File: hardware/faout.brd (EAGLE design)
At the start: 100 x 70 mm, 163 parts, among them IC2 MT48LC8M16A2, Q2 12MHz, Q3 MUN2214T1, Q4 MUN2214T1, Q5 ASFL, SW1 SMD_TACT_SWITCH, SW2 SMD_TACT_SWITCH, SW3 SMD_TACT_SWITCH, U1 93LC46BT-I/OT, U10 DAC8811DGK, U11 REF102AU, U12 DAC8811DGK, U13 ADR435ARZ, U14 AD8627AKSZ-R2, U15 OPA2277UA/2K5E4, U16 OPA2277UA/2K5E4, U17 MCP1700T-2502E/TT, U18 AD7980ARMZ, U2 LM3480IM3-3.3, U3 L7812ACV, U4 LM3671MF-3.3, U5 LM3671MF-1.2, U6 FLASH-SPI-25XXSMD1, U7 6SLX9TQG144, U8 AD8220ARMZ, U9 REF102AU, U99 L7912ACV

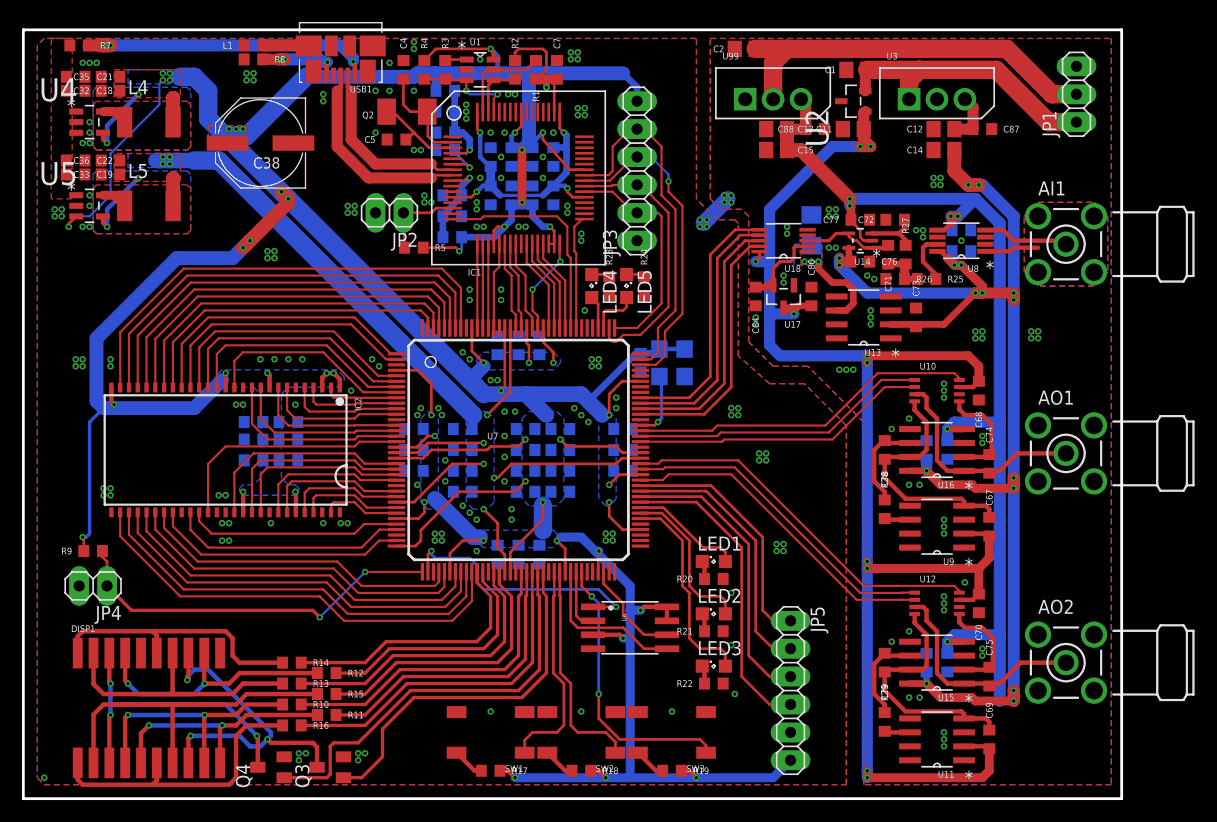
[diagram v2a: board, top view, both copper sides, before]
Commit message: Rearrange labels
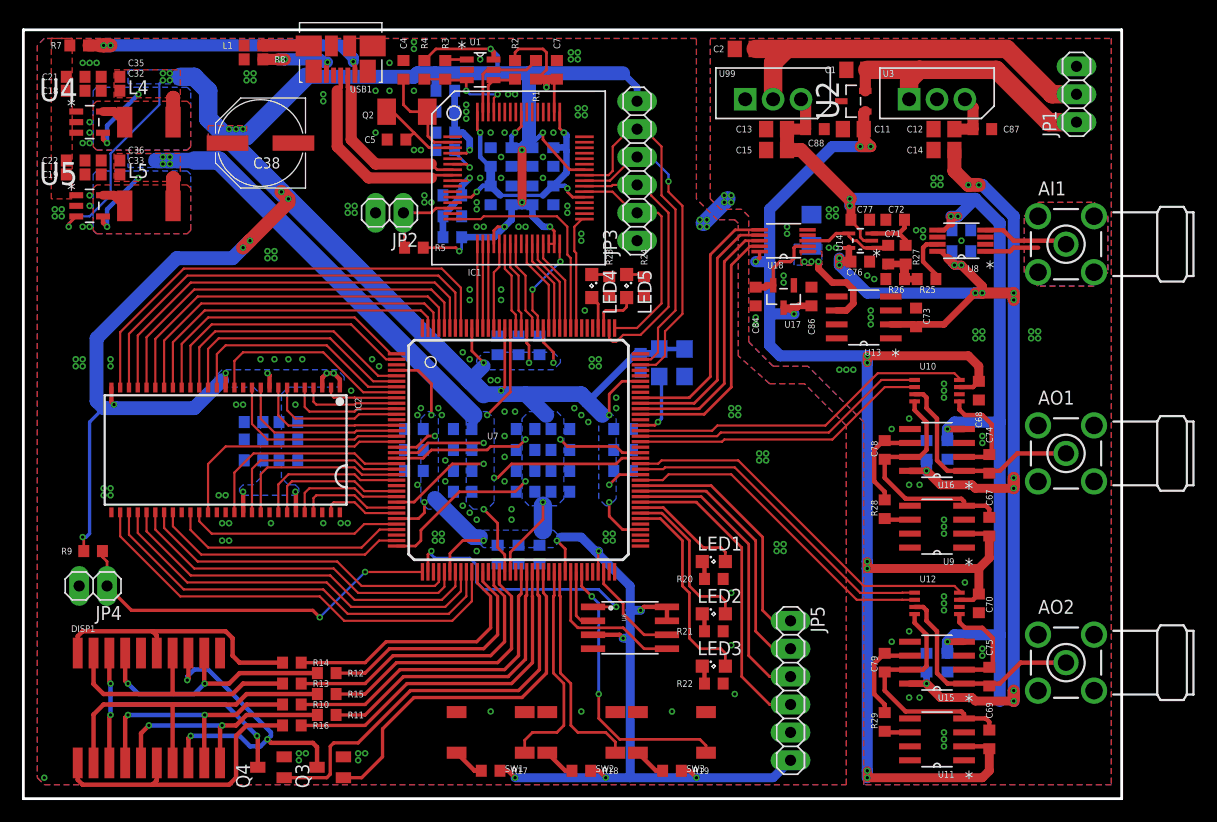
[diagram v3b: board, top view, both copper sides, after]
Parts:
- C85: device resistor:C1206 -> faout:R1206

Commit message: Cleanup and last adjustments.
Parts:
- removed C87, C88: 100nF, faout:R0603
- removed Q5: ASFL, crystal:ASF
- removed U99: L7912ACV, faout:TO254P450X1020X1935-3P
- added C8: 4.7uF, faout:R0603
- added C9: 100nF, faout:R0603
- added PWRLED1: (no value), led:SML0805
- added Q1: 12MHz, faout:TXC_QUARTZ_7A
- added R30: 2k, faout:R0603
- added U19: AD7980ARMZ, faout:SOP50P490X110-10N
- C6: value 4.7uF -> 100nF
- Q2: value 12MHz -> MUN2214T1; device faout:TXC_QUARTZ_7A -> transistor-npn:SC59-BEC
- Q4: value MUN2214T1 -> ASFL; device transistor-npn:SC59-BEC -> crystal:ASF
- R10: value 100 -> 4.7k
- R17: value 10k -> 100
- R20: value 300 -> 10k
- R25: value 7.47k -> 300
- R27: value 134k -> 7.47k
- R28: value 2k -> 134k
- R7: value 0 -> 300
- R9: value 4.7k -> 0
- U10, U12: value DAC8811DGK -> REF102AU; device faout:MSOP-8 -> faout:SOIC127P600X175-8N
- U11: value REF102AU -> DAC8811DGK; device faout:SOIC127P600X175-8N -> faout:MSOP-8
- U13: value ADR435ARZ -> DAC8811DGK; device faout:SOIC127P600X175-8N -> faout:MSOP-8
- U14: value AD8627AKSZ-R2 -> ADR435ARZ; device faout:SOT65P210X110-5N -> faout:SOIC127P600X175-8N
- U15: value OPA2277UA/2K5E4 -> AD8627AKSZ-R2; device faout:SOIC127P600X175-8N -> faout:SOT65P210X110-5N
- U17: value MCP1700T-2502E/TT -> OPA2277UA/2K5E4; device faout:SOT95P264X112-3N -> faout:SOIC127P600X175-8N
- U18: value AD7980ARMZ -> MCP1700T-2502E/TT; device faout:SOP50P490X110-10N -> faout:SOT95P264X112-3N
- U4: value LM3671MF-3.3 -> L7912ACV; device faout:SOT95P284X122-5N -> faout:TO254P450X1020X1935-3P
- U5: value LM3671MF-1.2 -> LM3671MF-3.3
- U6: value FLASH-SPI-25XXSMD1 -> LM3671MF-1.2; device GadgetFactory:SO08-EIAJ -> faout:SOT95P284X122-5N
- U7: value 6SLX9TQG144 -> M25PE16; device faout:TQ144 -> faout:SO8W
- U8: value AD8220ARMZ -> 6SLX9TQG144; device faout:SOP65P490X110-8N -> faout:TQ144
- U9: value REF102AU -> AD8220ARMZ; device faout:SOIC127P600X175-8N -> faout:SOP65P490X110-8N
- moved U4 64.8 mm to (70.8, 64.8)
- moved U6 62.4 mm to (6.03, 54.0), turned to 0 degrees
- moved Q2 60.1 mm to (27.9, 2.86), turned to 90 degrees
- moved Q4 51.9 mm to (59.1, 39.7), flipped to the bottom, turned to 270 degrees
- moved C6 48.9 mm to (87.3, 61.0), flipped to the top
- moved R9 47.1 mm to (21.0, 67.3), turned to 0 degrees
- moved U8 44.6 mm to (45.1, 31.8), turned to 0 degrees
- moved U15 39.0 mm to (76.2, 50.8)
- moved R23 37.4 mm to (62.9, 10.5), turned to 180 degrees
- moved U11 31.8 mm to (83.2, 37.1), turned to 0 degrees
- moved U13 26.9 mm to (83.2, 17.8), turned to 0 degrees
- moved U9 26.1 mm to (85.4, 50.8)
- moved R25 25.7 mm to (56.5, 46.7), turned to 90 degrees
- moved C7 24.1 mm to (72.1, 61.0), turned to 180 degrees
- moved R28 23.3 mm to (80.3, 49.5)
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- renumbered JP1 to PWR1, JP2 to USB_RST, JP3 to JTAG, JP4 to RST, JP5 to P1
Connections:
- new net N$26: PWRLED1.C, R7.2
- net !DAC1_CS: now also U11.8, U8.94; no longer U10.8, U7.94
- net !DAC2_CS: now also U13.8, U8.88; no longer U12.8, U7.88
- net !RAM_CAS: now also U8.5; no longer U7.5
- net !RAM_RAS: now also U8.2; no longer U7.2
- net !RAM_WE: now also U8.6; no longer U7.6
- net !USB_OE: now also U8.116; no longer U7.116
- net !USB_RD: now also U8.119; no longer U7.119
- net !USB_RXF: now also U8.121; no longer U7.121
- net !USB_TXE: now also U8.120; no longer U7.120
- net !USB_WR: now also U8.118; no longer U7.118
- net -15V: now also U4.2; no longer U99.2
- net 1V2: now also U6.4, U8.128, U8.19, U8.28, U8.52, U8.89; no longer U5.4, U7.128, U7.19, U7.28, U7.52, U7.89
- net 2V5: now also U19.2; no longer U17.2
- net 3V3: now also C9.1, PWRLED1.A, Q4.1, Q4.4, R10.2, R20.2, U5.4, U7.3, U7.7, U7.8, U8.103, U8.122, U8.125, U8.129, U8.135, U8.18, U8.20, U8.31, U8.36, U8.4, U8.42, U8.53, U8.63, U8.69, U8.76, U8.86, U8.90; no longer C7.1, Q5.1, Q5.4, R17.2, R9.2, U4.4, U5.3, U6.7, U6.8, U7.103, U7.122, U7.125, U7.129, U7.135, U7.18, U7.20, U7.31, U7.36, U7.4, U7.42, U7.53, U7.63, U7.69, U7.76, U7.86, U7.90
- net 5V0: now also R8.1, U5.3, U6.1; no longer R7.1, U4.1, U4.3
- net A+12V: now also C6.1, U14.2, U15.5, U17.8, U9.8; no longer C87.1, U13.2, U14.5, U15.8, U8.8
- net A+3V3: now also U10.2, U11.7, U12.2, U13.7, U18.3, U19.10; no longer U10.7, U11.2, U12.7, U17.3, U18.10, U9.2
- net A-12V: now also C7.2, U15.2, U17.4, U4.3, U9.5; no longer C88.2, U14.2, U15.4, U8.5, U99.3
- net ADC1_CNV: now also U19.6, U8.100; no longer U18.6, U7.100
- net ADC1_REF: now also U14.6, U19.1; no longer U13.6, U18.1
- net ADC1_SCK: now also U19.8, U8.98; no longer U18.8, U7.98
- net ADC1_SDI: now also U19.9, U8.97; no longer U18.9, U7.97
- net ADC1_SDO: now also U19.7, U8.99; no longer U18.7, U7.99
- net BUTTON1: now also U8.61; no longer U7.61
- net BUTTON2: now also U8.62; no longer U7.62
- net BUTTON3: now also U8.66; no longer U7.66
- net CLK_IN: now also Q4.3, U8.95; no longer Q5.3, U7.95
- net DAC1_CLK: now also U11.1, U8.93; no longer U10.1, U7.93
- net DAC1_IOUT: now also U11.5, U17.2; no longer U10.5, U16.2
- net DAC1_SDI: now also U11.2, U8.92; no longer U10.2, U7.92
- net DAC1_VOUT: now also U11.3, U17.1; no longer U10.3, U16.1
- net DAC1_VREF: now also U11.4, U17.7; no longer U16.7, U9.4
- net DAC1_VREFOUT: now also R29.2, U17.6; no longer R28.2, U16.6
- net DAC2_CLK: now also U13.1, U8.87; no longer U12.1, U7.87
- net DAC2_IOUT: now also U13.5, U16.2; no longer U12.5, U15.2
- net DAC2_SDI: now also U13.2, U8.85; no longer U12.2, U7.85
- net DAC2_VOUT: now also U13.3, U16.1; no longer U12.3, U15.1
- net DAC2_VREF: now also U13.4, U16.7; no longer U11.4, U15.7
- net DAC2_VREFOUT: now also R30.2, U16.6; no longer R29.2, U15.6
- net DISP_A: now also R11.2, U8.55; no longer R10.2, U7.55
- net DISP_B: now also R12.2, U8.56; no longer R11.2, U7.56
- net DISP_C: now also R13.2, U8.48; no longer R12.2, U7.48
- net DISP_CAT1: now also Q3.C; no longer Q4.C
- net DISP_D: now also R14.2, U8.50; no longer R13.2, U7.50
- net DISP_E: now also R15.2, U8.47; no longer R14.2, U7.47
- net DISP_EN1: now also Q3.B, U8.58; no longer Q4.B, U7.58
- net DISP_EN2: now also Q2.B, U8.59; no longer Q3.B, U7.59
- net DISP_F: now also R16.2, U8.51; no longer R15.2, U7.51
- net DISP_G: now also R17.2, U8.57; no longer R16.2, U7.57
- net DISP_INT_A: now also R11.1; no longer R10.1
- net DISP_INT_B: now also R12.1; no longer R11.1
- net DISP_INT_C: now also R13.1; no longer R12.1
- net DISP_INT_D: now also R14.1; no longer R13.1
- net DISP_INT_E: now also R15.1; no longer R14.1
- net DISP_INT_F: now also R16.1; no longer R15.1
- net DISP_INT_G: now also R17.1; no longer R16.1
- net FLASH_CS: now also U7.1, U8.38; no longer U6.1, U7.38
- net FLASH_MISO: now also U7.2, U8.65; no longer U6.2, U7.65
- net FLASH_MOSI: now also U7.5, U8.64; no longer U6.5, U7.64
- net FLASH_SCK: now also U7.6, U8.70; no longer U6.6, U7.70
- net GND: now also C7.1, C8.2, C9.2, Q2.E, Q4.2, R25.1, R27.1, R7.1, R9.1, U11.6, U13.6, U14.4, U17.3, U17.5, U18.1, U19.4, U19.5, U4.1, U6.2, U7.4, U8.108, U8.113, U8.13, U8.130, U8.136, U8.144, U8.25, U8.3, U8.49, U8.54, U8.60, U8.68, U8.73, U8.77, U8.91, U8.96, U9.6; no longer C7.2, C87.2, C88.1, Q4.E, Q5.2, R20.1, R26.1, R8.1, U10.6, U12.6, U13.4, U15.3, U15.5, U17.1, U18.4, U18.5, U4.2, U6.4, U7.108, U7.113, U7.13, U7.130, U7.136, U7.144, U7.25, U7.3, U7.49, U7.54, U7.60, U7.68, U7.73, U7.77, U7.91, U7.96, U8.6, U99.1
- net JP_1: now also U8.84; no longer U7.84
- net JP_2: now also U8.83; no longer U7.83
- net JP_3: now also U8.82; no longer U7.82
- net JP_4: now also U8.81; no longer U7.81
- net LED1: now also U8.80; no longer U7.80
- net LED2: now also U8.79; no longer U7.79
- net LED3: now also U8.78; no longer U7.78
- net LED_4: now also U8.112; no longer U7.112
- net LED_5: now also U8.111; no longer U7.111
- net N$1: now also Q1.1; no longer Q2.1
- net N$10: now also R29.1, U10.6; no longer R28.1, U9.6
- net N$11: now also U9.1; no longer U8.1
- net N$12: now also U15.1, U15.4, U19.3; no longer U14.1, U14.4, U18.3
- net N$13: now also R26.2, U9.7; no longer R25.2, U8.7
- net N$14: now also R26.1, R27.2, R28.1; no longer R25.1, R26.2, R27.1
- net N$15: now also R28.2, U15.3; no longer R27.2, U14.3
- net N$17: now also Q2.C; no longer Q3.C
- net N$18: now also R18.1; no longer R17.1
- net N$19: now also R19.1; no longer R18.1
- net N$2: now also Q1.2; no longer Q2.2
- net N$20: now also R20.1; no longer R19.1
- net N$21: now also R21.2; no longer R20.2
- net N$22: now also R22.2; no longer R21.2
- net N$23: now also R23.2; no longer R22.2
- net N$24: now also U5.5; no longer U4.5
- net N$25: now also U6.5; no longer U5.5
- net N$3: now also R24.2; no longer R23.2
- net N$4: now also R25.2; no longer R24.2
- net N$5: now also C8.1; no longer C6.1
- net N$8: now also R30.1, U12.6; no longer R29.1, U11.6
- net N$9: now also U9.4; no longer U8.4
- net RAM_A0: now also U8.140; no longer U7.140
- net RAM_A1: now also U8.139; no longer U7.139
- net RAM_A10: now also U8.141; no longer U7.141
- net RAM_A11: now also U8.35; no longer U7.35
- net RAM_A2: now also U8.138; no longer U7.138
- net RAM_A3: now also U8.137; no longer U7.137
- net RAM_A4: now also U8.46; no longer U7.46
- net RAM_A5: now also U8.45; no longer U7.45
- net RAM_A6: now also U8.44; no longer U7.44
- net RAM_A7: now also U8.43; no longer U7.43
- net RAM_A8: now also U8.41; no longer U7.41
- net RAM_A9: now also U8.40; no longer U7.40
- net RAM_BA0: now also U8.143; no longer U7.143
- net RAM_BA1: now also U8.142; no longer U7.142
- net RAM_CKE: now also U8.33; no longer U7.33
- net RAM_CLK: now also U8.32; no longer U7.32
- net RAM_CS: now also U8.1; no longer U7.1
- net RAM_DQ0: now also U8.9; no longer U7.9
- net RAM_DQ1: now also U8.10; no longer U7.10
- net RAM_DQ10: now also U8.23; no longer U7.23
- net RAM_DQ11: now also U8.24; no longer U7.24
- net RAM_DQ12: now also U8.26; no longer U7.26
- net RAM_DQ13: now also U8.27; no longer U7.27
- net RAM_DQ14: now also U8.29; no longer U7.29
- net RAM_DQ15: now also U8.30; no longer U7.30
- net RAM_DQ2: now also U8.11; no longer U7.11
- net RAM_DQ3: now also U8.12; no longer U7.12
- net RAM_DQ4: now also U8.14; no longer U7.14
- net RAM_DQ5: now also U8.15; no longer U7.15
- net RAM_DQ6: now also U8.16; no longer U7.16
- net RAM_DQ7: now also U8.8; no longer U7.8
- net RAM_DQ8: now also U8.21; no longer U7.21
- net RAM_DQ9: now also U8.22; no longer U7.22
- net RAM_DQMH: now also U8.17; no longer U7.17
- net RAM_DQML: now also U8.7; no longer U7.7
- net RESET: now also R10.1, U8.37; no longer R9.1, U7.37
- net TCK: now also U8.109; no longer U7.109
- net TDI: now also U8.110; no longer U7.110
- net TDO: now also U8.106; no longer U7.106
- net TMS: now also U8.107; no longer U7.107
- net USB_CLKOUT: now also U8.123; no longer U7.123
- net USB_D0: now also U8.117; no longer U7.117
- net USB_D1: now also U8.134; no longer U7.134
- net USB_D2: now also U8.133; no longer U7.133
- net USB_D3: now also U8.132; no longer U7.132
- net USB_D4: now also U8.131; no longer U7.131
- net USB_D5: now also U8.127; no longer U7.127
- net USB_D6: now also U8.126; no longer U7.126
- net USB_D7: now also U8.124; no longer U7.124
- net USB_GND: now also R9.2; no longer R8.2
- net USB_V: now also R8.2; no longer R7.2
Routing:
- net N$26: track 0.00 -> 1.67 mm
- net 3V3: track 448.7 -> 450.4 mm
- net A+12V: track 122.1 -> 122.7 mm
- net GND: vias 241 -> 240
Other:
- board text added: "+15V"
- board text added: "-15V"
- board text added: "1"
- board text added: "2"
- board text added: "3"
- board text added: "3V3"
- board text added: "4"
- board text added: "FT2232H"
- board text added: "GND"
- board text added: "SDRAM"
- board text added: "Spartan 6 LX9"
- board text added: "TCK"
- board text added: "TDI"
- board text added: "TDO"
- board text added: "TMS"

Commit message: Fix display orientation and start production.
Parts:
- R5: value 1k -> 10k
- moved P1 0.63 mm to (69.2, 9.84)
- renumbered DISP1 to DISP, PWR1 to APWR, PWRLED1 to PWR
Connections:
- net N$17 renamed DISP_CAT2
- net DISP_A: now also R14.2, U8.50; no longer R11.2, U8.55
- net DISP_B: now also R13.2, U8.48; no longer R12.2, U8.56
- net DISP_C: now also R12.2, U8.56; no longer R13.2, U8.48
- net DISP_D: now also R11.2, U8.55; no longer R14.2, U8.50
- net DISP_E: now also R17.2, U8.57; no longer R15.2, U8.47
- net DISP_G: now also R15.2, U8.47; no longer R17.2, U8.57
- net DISP_INT_A: now also R14.1; no longer R11.1
- net DISP_INT_B: now also R13.1; no longer R12.1
- net DISP_INT_C: now also R12.1; no longer R13.1
- net DISP_INT_D: now also R11.1; no longer R14.1
- net DISP_INT_E: now also R17.1; no longer R15.1
- net DISP_INT_G: now also R15.1; no longer R17.1
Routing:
- net DISP_G: track 31.7 -> 24.2 mm
- net DISP_E: track 24.2 -> 31.7 mm
- net DISP_C: track 22.4 -> 27.3 mm
- net DISP_B: track 27.3 -> 22.4 mm
- net DISP_INT_F: track 30.9 -> 27.7 mm
- net DISP_INT_A: track 23.3 -> 20.5 mm
- net DISP_D: track 26.9 -> 29.4 mm
- net DISP_A: track 29.4 -> 26.9 mm
- net DISP_INT_G: track 27.0 -> 24.6 mm
- net DISP_INT_E: track 24.6 -> 26.5 mm
- net DISP_INT_B: track 22.9 -> 21.9 mm
- net 3V3: track 450.4 -> 449.7 mm, vias 53 -> 55
- net 1V2: vias 11 -> 13
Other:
- board text added: "FPGA - Analog In/Out Evaluation Board"
- board text added: "TU KL (05/2014)"
- board text removed: "SDRAM"
